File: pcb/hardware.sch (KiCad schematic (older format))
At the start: 54 parts, among them U2 A33

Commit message: Sync
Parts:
- removed C32, C34, C46, C50: 100nF, Capacitor_SMD:C_0402_1005Metric, symbol Device:C_Small
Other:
- moved on the sheet: C54
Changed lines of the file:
@@
 	1    0    0    -1
 $EndComp
-$Comp
-L Device:C_Small C?
-U 1 1 609FF0BF
-P 4600 2700
-AR Path="/60536DA4/609FF0BF" Ref="C?"  Part="1"
-AR Path="/609FF0BF" Ref="C32"  Part="1"
-F 0 "C32" V 4650 2750 50  0000 L CNN
-F 1 "100nF" V 4550 2750 50  0000 L CNN
-F 2 "Capacitor_SMD:C_0402_1005Metric" H 4600 2700 50  0001 C CNN
-F 3 "~" H 4600 2700 50  0001 C CNN
-	1    4600 2700
-	1    0    0    -1
-$EndComp
-Wire Wire Line
-	4600 2600 4600 2350
-Wire Wire Line
-	4600 2350 4800 2350
 Wire Wire Line
 	5200 2350 5200 2300
-$Comp
-L Device:C_Small C?
-U 1 1 609FF0C8
-P 4800 2700
-AR Path="/60536DA4/609FF0C8" Ref="C?"  Part="1"
-AR Path="/609FF0C8" Ref="C34"  Part="1"
-F 0 "C34" V 4850 2750 50  0000 L CNN
-F 1 "100nF" V 4750 2750 50  0000 L CNN
-F 2 "Capacitor_SMD:C_0402_1005Metric" H 4800 2700 50  0001 C CNN
-F 3 "~" H 4800 2700 50  0001 C CNN
-	1    4800 2700
-	1    0    0    -1
-$EndComp
 $Comp
 L Device:C_Small C?
@@
 $Comp
 L Device:C_Small C?
-U 1 1 609FF0DA
+U 1 1 609FF0E6
 P 5400 2700
-AR Path="/60536DA4/609FF0DA" Ref="C?"  Part="1"
-AR Path="/609FF0DA" Ref="C46"  Part="1"
-F 0 "C46" V 5450 2750 50  0000 L CNN
-F 1 "100nF" V 5350 2750 50  0000 L CNN
+AR Path="/60536DA4/609FF0E6" Ref="C?"  Part="1"
+AR Path="/609FF0E6" Ref="C54"  Part="1"
+F 0 "C54" V 5450 2750 50  0000 L CNN
+F 1 "22uF" V 5350 2750 50  0000 L CNN
 F 2 "Capacitor_SMD:C_0402_1005Metric" H 5400 2700 50  0001 C CNN
 F 3 "~" H 5400 2700 50  0001 C CNN
@@
 	1    0    0    -1
 $EndComp
-$Comp
-L Device:C_Small C?
-U 1 1 609FF0E0
-P 5600 2700
-AR Path="/60536DA4/609FF0E0" Ref="C?"  Part="1"
-AR Path="/609FF0E0" Ref="C50"  Part="1"
-F 0 "C50" V 5650 2750 50  0000 L CNN
-F 1 "100nF" V 5550 2750 50  0000 L CNN
-F 2 "Capacitor_SMD:C_0402_1005Metric" H 5600 2700 50  0001 C CNN
-F 3 "~" H 5600 2700 50  0001 C CNN
-	1    5600 2700
-	1    0    0    -1
-$EndComp
-$Comp
-L Device:C_Small C?
-U 1 1 609FF0E6
-P 5800 2700
-AR Path="/60536DA4/609FF0E6" Ref="C?"  Part="1"
-AR Path="/609FF0E6" Ref="C54"  Part="1"
-F 0 "C54" V 5850 2750 50  0000 L CNN
-F 1 "22uF" V 5750 2750 50  0000 L CNN
-F 2 "Capacitor_SMD:C_0402_1005Metric" H 5800 2700 50  0001 C CNN
-F 3 "~" H 5800 2700 50  0001 C CNN
-	1    5800 2700
-	1    0    0    -1
-$EndComp
-Wire Wire Line
-	5200 2350 5400 2350
-Wire Wire Line
-	5800 2350 5800 2600
+Wire Wire Line
+	5400 2350 5400 2600
 Connection ~ 5200 2350
 Wire Wire Line
-	5600 2600 5600 2350
-Connection ~ 5600 2350
-Wire Wire Line
-	5600 2350 5800 2350
-Wire Wire Line
-	5400 2600 5400 2350
-Connection ~ 5400 2350
-Wire Wire Line
-	5400 2350 5600 2350
-Wire Wire Line
 	5200 2600 5200 2350
 Wire Wire Line
 	5000 2600 5000 2350
-Connection ~ 5000 2350
 Wire Wire Line
 	5000 2350 5200 2350
 Wire Wire Line
-	4800 2600 4800 2350
-Connection ~ 4800 2350
-Wire Wire Line
-	4800 2350 5000 2350
-Wire Wire Line
-	4600 2800 4600 2900
-Wire Wire Line
-	4600 2900 4800 2900
-Wire Wire Line
-	5800 2900 5800 2800
-Wire Wire Line
-	5600 2800 5600 2900
-Connection ~ 5600 2900
-Wire Wire Line
-	5600 2900 5800 2900
-Wire Wire Line
-	5400 2800 5400 2900
-Connection ~ 5400 2900
-Wire Wire Line
-	5400 2900 5600 2900
+	5400 2900 5400 2800
 Wire Wire Line
 	5200 2800 5200 2900
 Connection ~ 5200 2900
 Wire Wire Line
-	5200 2900 5400 2900
-Wire Wire Line
 	5000 2800 5000 2900
-Connection ~ 5000 2900
 Wire Wire Line
 	5000 2900 5200 2900
-Wire Wire Line
-	4800 2800 4800 2900
-Connection ~ 4800 2900
-Wire Wire Line
-	4800 2900 5000 2900
 $Comp
 L power:GND #PWR?
@@
 	0    1    1    0
 $EndComp
+Wire Wire Line
+	5200 2350 5400 2350
+Wire Wire Line
+	5400 2900 5200 2900
 Wire Bus Line
 	3950 3400 3950 3600

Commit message: Working on the power supplies
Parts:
- removed C35, C36, C39, C41, C44, C45, C47, C49, C51, C52, C63: 100nF, Capacitor_SMD:C_0402_1005Metric, symbol Device:C_Small
- removed C57, C58, C71: 22uF, Capacitor_SMD:C_0402_1005Metric, symbol Device:C_Small
- C55, C56, C69: value 100nF -> 22uF
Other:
- moved on the sheet: C31, C33, C37, C40, C53, C55, C56, C59, C61

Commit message: Working on the routing.
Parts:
- removed C60, C62: 100nF, Capacitor_SMD:C_0402_1005Metric, symbol Device:C_Small
- removed C72: 22uF, Capacitor_SMD:C_0402_1005Metric, symbol Device:C_Small
- C70: value 100nF -> 22uF
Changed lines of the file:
@@
-	1    0    0    -1
-$EndComp
-$Comp
-L Device:C_Small C?
-U 1 1 60B9DBD6
-P 6350 4800
-AR Path="/60536DA4/60B9DBD6" Ref="C?"  Part="1"
-AR Path="/60B9DBD6" Ref="C60"  Part="1"
-F 0 "C60" V 6400 4850 50  0000 L CNN
-F 1 "100nF" V 6300 4850 50  0000 L CNN
-F 2 "Capacitor_SMD:C_0402_1005Metric" H 6350 4800 50  0001 C CNN
-F 3 "~" H 6350 4800 50  0001 C CNN
-	1    6350 4800
 	1    0    0    -1
 $EndComp
 Wire Wire Line
-	6350 4700 6350 4450
-Wire Wire Line
-	6350 4450 6550 4450
-Wire Wire Line
 	6950 4450 6950 4400
-$Comp
-L Device:C_Small C?
-U 1 1 60B9DBDF
-P 6550 4800
-AR Path="/60536DA4/60B9DBDF" Ref="C?"  Part="1"
-AR Path="/60B9DBDF" Ref="C62"  Part="1"
-F 0 "C62" V 6600 4850 50  0000 L CNN
-F 1 "100nF" V 6500 4850 50  0000 L CNN
-F 2 "Capacitor_SMD:C_0402_1005Metric" H 6550 4800 50  0001 C CNN
-F 3 "~" H 6550 4800 50  0001 C CNN
-	1    6550 4800
-	1    0    0    -1
-$EndComp
 $Comp
 L Device:C_Small C?
@@
 AR Path="/60B9DBF7" Ref="C70"  Part="1"
 F 0 "C70" V 7400 4850 50  0000 L CNN
-F 1 "100nF" V 7300 4850 50  0000 L CNN
+F 1 "22uF" V 7300 4850 50  0000 L CNN
 F 2 "Capacitor_SMD:C_0402_1005Metric" H 7350 4800 50  0001 C CNN
 F 3 "~" H 7350 4800 50  0001 C CNN
@@
 	1    0    0    -1
 $EndComp
-$Comp
-L Device:C_Small C?
-U 1 1 60B9DBFD
-P 7550 4800
-AR Path="/60536DA4/60B9DBFD" Ref="C?"  Part="1"
-AR Path="/60B9DBFD" Ref="C72"  Part="1"
-F 0 "C72" V 7600 4850 50  0000 L CNN
-F 1 "22uF" V 7500 4850 50  0000 L CNN
-F 2 "Capacitor_SMD:C_0402_1005Metric" H 7550 4800 50  0001 C CNN
-F 3 "~" H 7550 4800 50  0001 C CNN
-	1    7550 4800
-	1    0    0    -1
-$EndComp
 Wire Wire Line
 	6950 4450 7150 4450
-Wire Wire Line
-	7550 4450 7550 4700
 Connection ~ 6950 4450
 Wire Wire Line
 	7350 4700 7350 4450
-Connection ~ 7350 4450
-Wire Wire Line
-	7350 4450 7550 4450
 Wire Wire Line
 	7150 4700 7150 4450
@@
 Wire Wire Line
 	6750 4700 6750 4450
-Connection ~ 6750 4450
 Wire Wire Line
 	6750 4450 6950 4450
 Wire Wire Line
-	6550 4700 6550 4450
-Connection ~ 6550 4450
-Wire Wire Line
-	6550 4450 6750 4450
-Wire Wire Line
-	6350 4900 6350 5000
-Wire Wire Line
-	6350 5000 6550 5000
-Wire Wire Line
-	7550 5000 7550 4900
-Wire Wire Line
 	7350 4900 7350 5000
-Connection ~ 7350 5000
-Wire Wire Line
-	7350 5000 7550 5000
 Wire Wire Line
 	7150 4900 7150 5000
@@
 Wire Wire Line
 	6750 4900 6750 5000
-Connection ~ 6750 5000
 Wire Wire Line
 	6750 5000 6950 5000
-Wire Wire Line
-	6550 4900 6550 5000
-Connection ~ 6550 5000
-Wire Wire Line
-	6550 5000 6750 5000
 $Comp
 L power:GND #PWR?

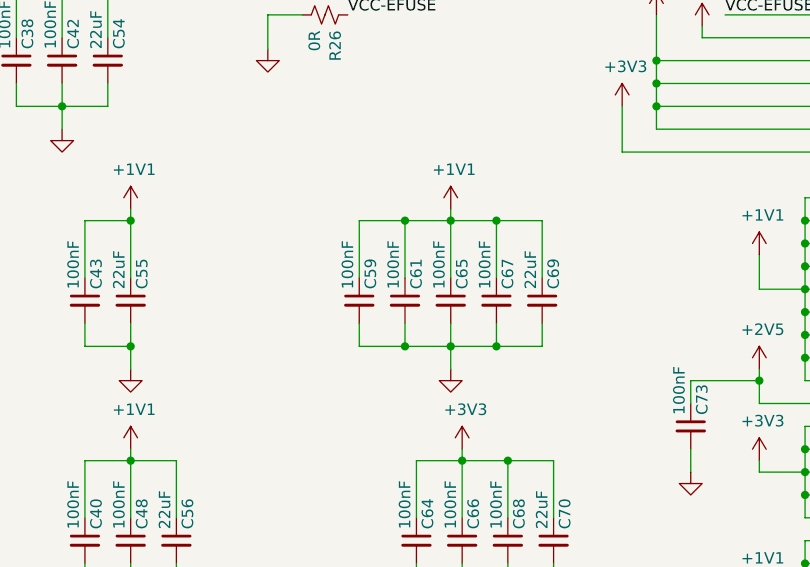
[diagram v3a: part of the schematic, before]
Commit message: Routing power supplies
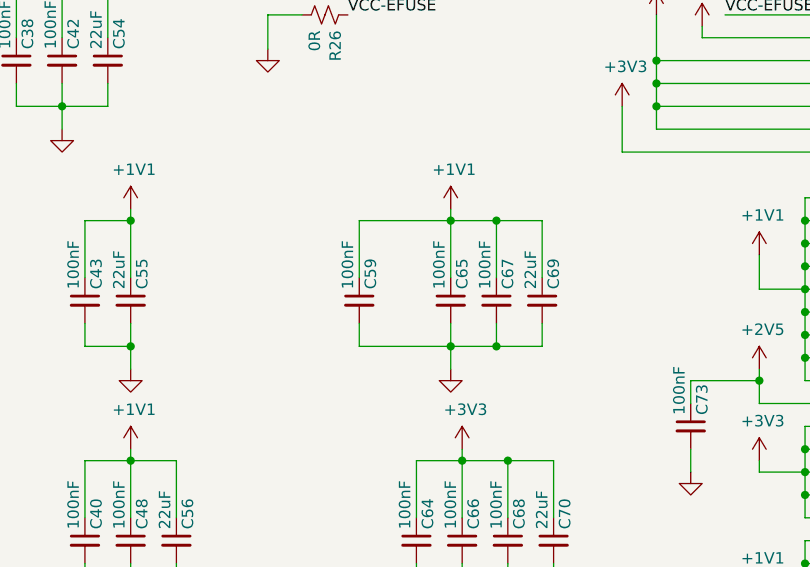
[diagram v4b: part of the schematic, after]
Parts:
- removed C61: 100nF, Capacitor_SMD:C_0402_1005Metric, symbol Device:C_Small
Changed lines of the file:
@@
-$Comp
-L Device:C_Small C?
-U 1 1 60AEEC72
-P 6700 3750
-AR Path="/60536DA4/60AEEC72" Ref="C?"  Part="1"
-AR Path="/60AEEC72" Ref="C61"  Part="1"
-F 0 "C61" V 6750 3800 50  0000 L CNN
-F 1 "100nF" V 6650 3800 50  0000 L CNN
-F 2 "Capacitor_SMD:C_0402_1005Metric" H 6700 3750 50  0001 C CNN
-F 3 "~" H 6700 3750 50  0001 C CNN
-	1    6700 3750
-	1    0    0    -1
-$EndComp
 $Comp
 L Device:C_Small C?
@@
 	6900 3650 6900 3400
 Wire Wire Line
-	6700 3650 6700 3400
-Wire Wire Line
 	6500 3850 6500 3950
 Wire Wire Line
@@
 Wire Wire Line
 	6900 3950 7100 3950
-Wire Wire Line
-	6700 3850 6700 3950
 $Comp
 L power:GND #PWR?
@@
 	5300 5000 5500 5000
 Wire Wire Line
-	6500 3400 6700 3400
-Wire Wire Line
-	6500 3950 6700 3950
-Connection ~ 6700 3400
-Wire Wire Line
-	6700 3400 6900 3400
-Connection ~ 6700 3950
-Wire Wire Line
-	6700 3950 6900 3950
+	6500 3400 6900 3400
+Wire Wire Line
+	6500 3950 6900 3950
 Wire Bus Line
 	3950 3400 3950 3600

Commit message: Working on silkscreen/placement
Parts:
- added H1, H2, H3, H4: MountingHole, MountingHole:MountingHole_3.2mm_M3, symbol Mechanical:MountingHole
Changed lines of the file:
@@
 adr14
 $Sheet
-S 5400 6500 1450 1100
+S 4800 6000 1450 1100
 U 6063BE69
 F0 "gpio" 50
@@
 Wire Bus Line
 	4050 1700 4050 3300
+$Comp
+L Mechanical:MountingHole H2
+U 1 1 60922768
+P 750 7150
+F 0 "H2" H 850 7196 50  0000 L CNN
+F 1 "MountingHole" H 850 7105 50  0000 L CNN
+F 2 "MountingHole:MountingHole_3.2mm_M3" H 750 7150 50  0001 C CNN
+F 3 "~" H 750 7150 50  0001 C CNN
+	1    750  7150
+	1    0    0    -1
+$EndComp
+$Comp
+L Mechanical:MountingHole H3
+U 1 1 60924423
+P 750 7350
+F 0 "H3" H 850 7396 50  0000 L CNN
+F 1 "MountingHole" H 850 7305 50  0000 L CNN
+F 2 "MountingHole:MountingHole_3.2mm_M3" H 750 7350 50  0001 C CNN
+F 3 "~" H 750 7350 50  0001 C CNN
+	1    750  7350
+	1    0    0    -1
+$EndComp
+$Comp
+L Mechanical:MountingHole H4
+U 1 1 60924734
+P 750 7550
+F 0 "H4" H 850 7596 50  0000 L CNN
+F 1 "MountingHole" H 850 7505 50  0000 L CNN
+F 2 "MountingHole:MountingHole_3.2mm_M3" H 750 7550 50  0001 C CNN
+F 3 "~" H 750 7550 50  0001 C CNN
+	1    750  7550
+	1    0    0    -1
+$EndComp
+$Comp
+L Mechanical:MountingHole H1
+U 1 1 609248F0
+P 750 6950
+F 0 "H1" H 850 6996 50  0000 L CNN
+F 1 "MountingHole" H 850 6905 50  0000 L CNN
+F 2 "MountingHole:MountingHole_3.2mm_M3" H 750 6950 50  0001 C CNN
+F 3 "~" H 750 6950 50  0001 C CNN
+	1    750  6950
+	1    0    0    -1
+$EndComp
 $EndSCHEMATC
